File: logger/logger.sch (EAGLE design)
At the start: 18 parts, among them IC1 75176AD, U1 MSP430G2352IPW14

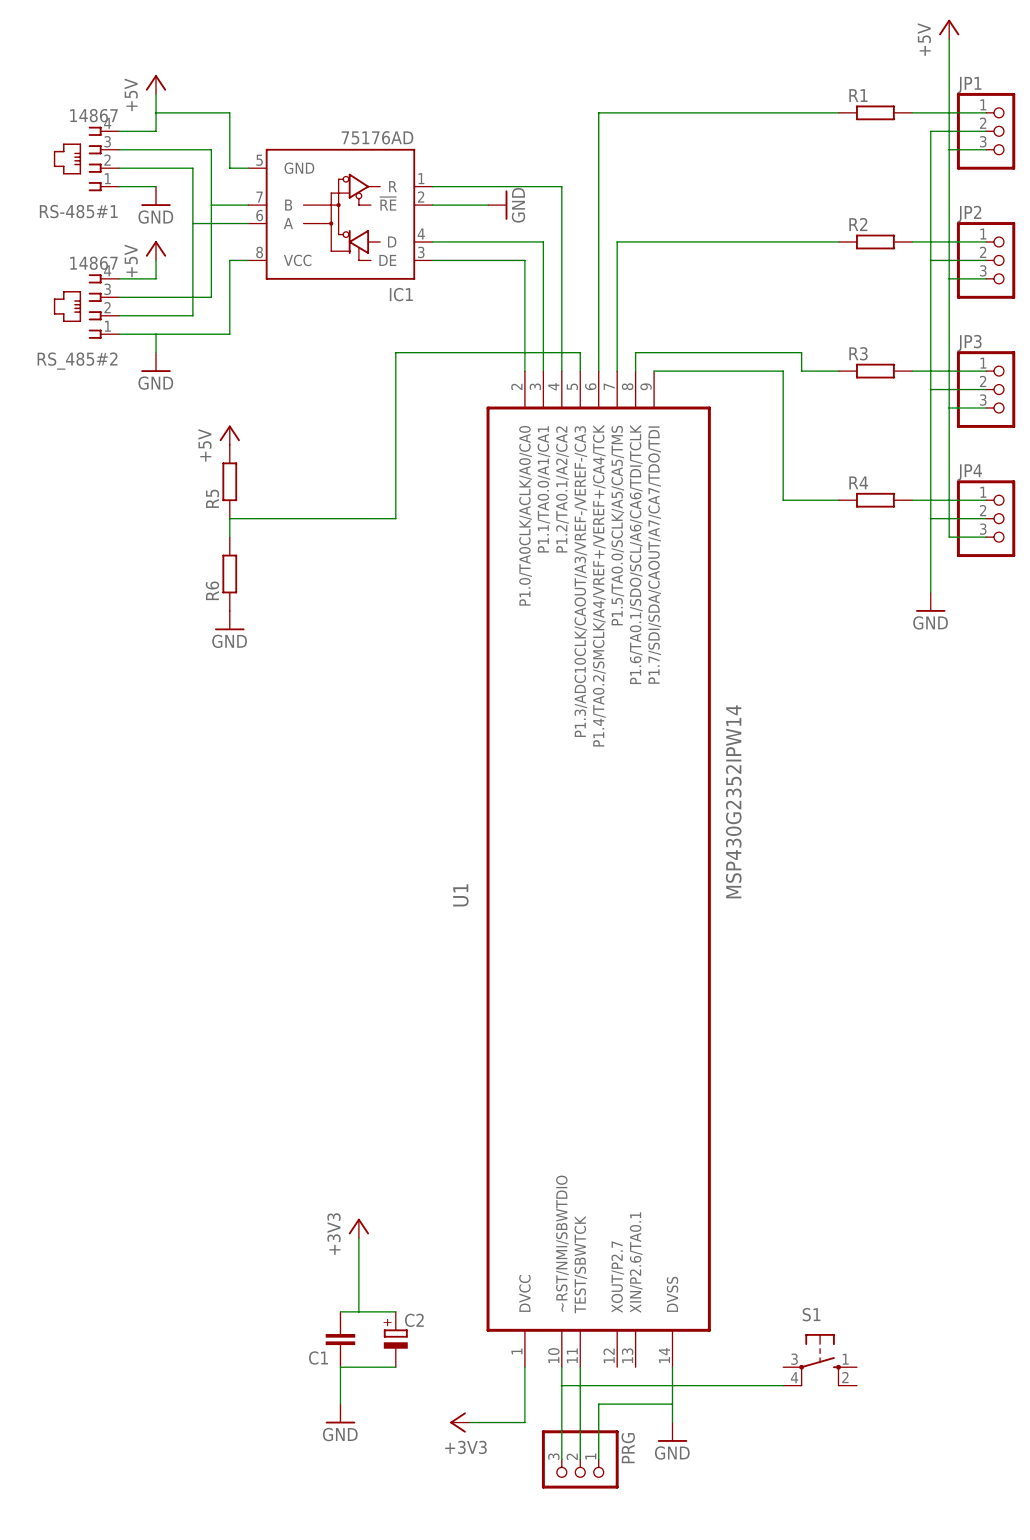
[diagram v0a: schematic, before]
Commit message: Bugfixes, partially routed.
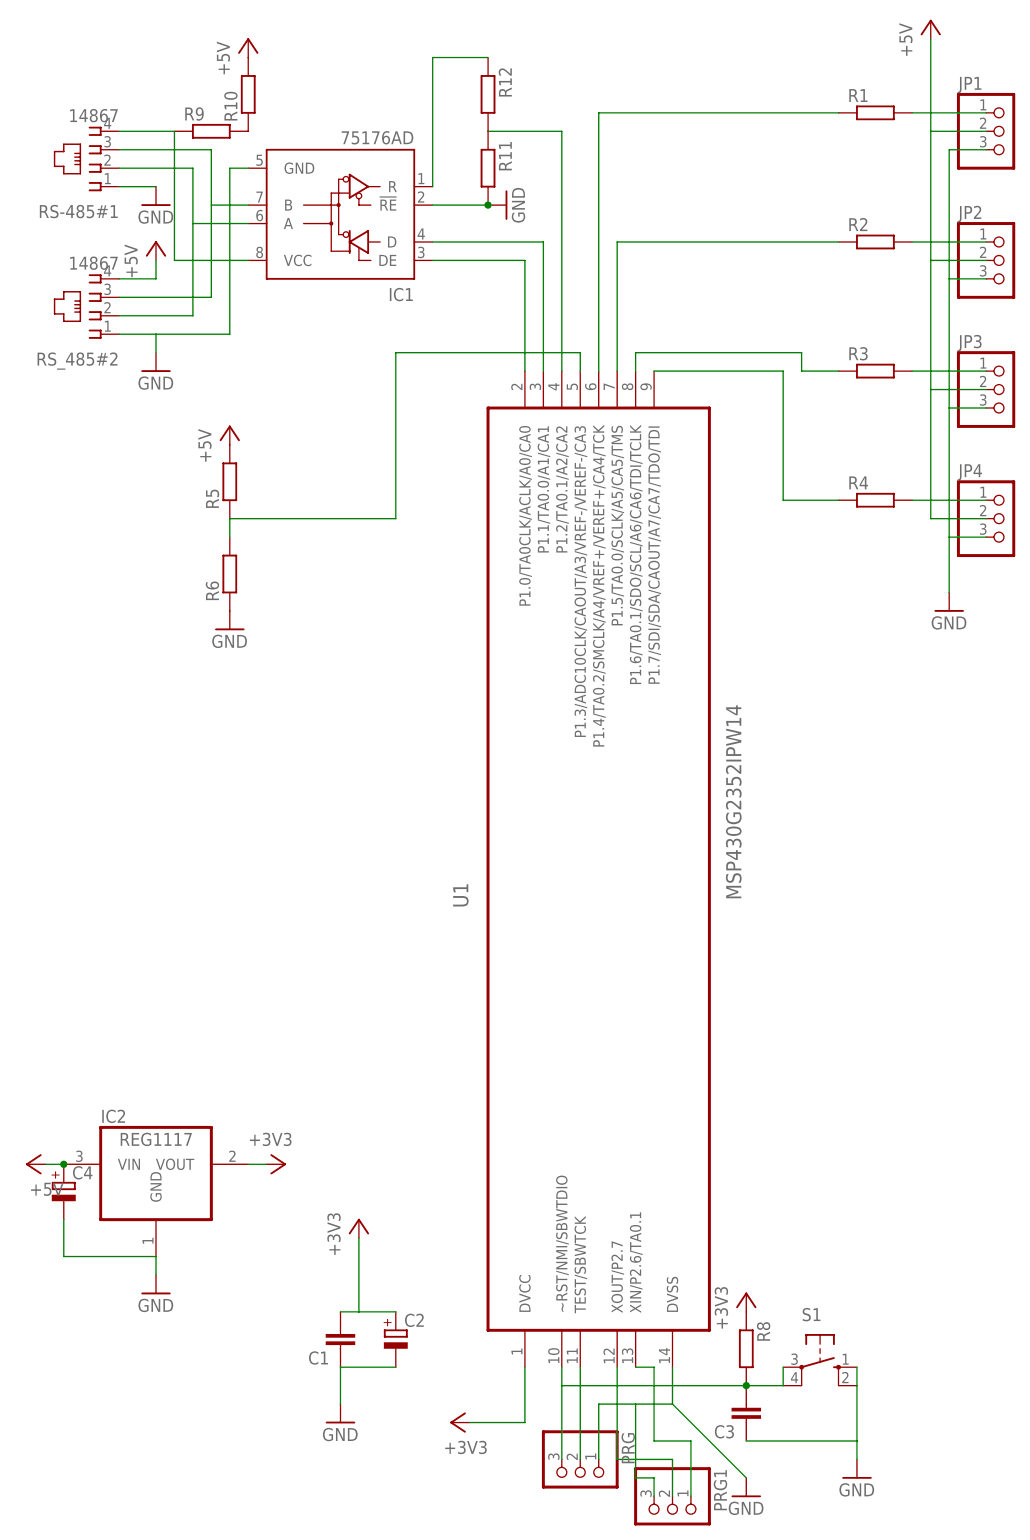
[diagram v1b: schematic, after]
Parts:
- added C3: (no value), rcl:C-EUC0805
- added C4: (no value), rcl:CPOL-EUE2,5-6E
- added IC2: REG1117, burr-brown:REG1117
- added PRG1: (no value), pinhead:PINHD-1X3
- added R10, R9: (no value), rcl:R-EU_R1206
- added R11, R12, R8: (no value), rcl:R-EU_R0805
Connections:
- removed net N$12: IC1.R, U1.P1.2/TA0.1/A2/CA2
- new net N$17: PRG1.1, U1.XIN/P2.6/TA0.1
- new net N$18: PRG1.2, U1.XOUT/P2.7
- new net N$19: R10.1, R9.2
- new net N$20: IC1.VCC, R9.1, RS-485#1.4
- new net N$21: IC1.R, R12.1
- new net N$22: R11.1, R12.2, U1.P1.2/TA0.1/A2/CA2
- net +3V3: now also IC2.VOUT, R8.1
- net +5V: now also C4.+, IC2.VIN, JP1.2, JP2.2, JP3.2, JP4.2, R10.2; no longer IC1.GND, JP1.3, JP2.3, JP3.3, JP4.3, RS-485#1.4
- net GND: now also C3.1, C4.-, IC1.GND, IC2.GND, JP1.3, JP2.3, JP3.3, JP4.3, PRG1.3, R11.2, S1.S, S1.S1; no longer IC1.VCC, JP1.2, JP2.2, JP3.2, JP4.2
- net N$15: now also C3.2, R8.2, S1.P

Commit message: Routed.
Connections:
- removed net N$17: PRG1.1, U1.XIN/P2.6/TA0.1
- new net N$12: PRG1.2, U1.XIN/P2.6/TA0.1
- net +3V3: now also IC2.VOUT_P
- net GND: now also PRG1.1; no longer PRG1.3
- net N$18: now also PRG1.3; no longer PRG1.2
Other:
- moved on the sheet: C1, C2
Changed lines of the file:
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@@
 <part name="C1" library="rcl" deviceset="C-EU" device="C0805"/>
 <part name="C2" library="rcl" deviceset="CPOL-EU" device="E2,5-6E"/>
-<part name="+3V2" library="supply1" deviceset="+3V3" device=""/>
-<part name="GND7" library="supply1" deviceset="GND" device=""/>
 <part name="PRG" library="pinhead" deviceset="PINHD-1X3" device=""/>
 <part name="S1" library="switch-omron" deviceset="10-XX" device=""/>
@@
 <part name="R11" library="rcl" deviceset="R-EU_" device="R0805"/>
 <part name="R12" library="rcl" deviceset="R-EU_" device="R0805"/>
+<part name="C4" library="rcl" deviceset="CPOL-EU" device="E2,5-6E"/>
 <part name="IC2" library="burr-brown" deviceset="REG1117" device=""/>
-<part name="C4" library="rcl" deviceset="CPOL-EU" device="E2,5-6E"/>
 </parts>
 <sheets>
@@
 <instance part="+3V1" gate="G$1" x="40.64" y="-104.14" rot="R90"/>
 <instance part="GND6" gate="1" x="48.26" y="63.5" rot="R90"/>
-<instance part="C1" gate="G$1" x="25.4" y="-93.98" rot="R180"/>
-<instance part="C2" gate="G$1" x="33.02" y="-91.44"/>
-<instance part="+3V2" gate="G$1" x="27.94" y="-76.2"/>
-<instance part="GND7" gate="1" x="25.4" y="-104.14"/>
+<instance part="C1" gate="G$1" x="22.86" y="-73.66" rot="R180"/>
+<instance part="C2" gate="G$1" x="27.94" y="-71.12"/>
 <instance part="PRG" gate="A" x="58.42" y="-111.76" rot="R270"/>
 <instance part="S1" gate="1" x="91.44" y="-96.52" rot="R270"/>
 <instance part="GND8" gate="1" x="0" y="-86.36"/>
-<instance part="+3V3" gate="G$1" x="17.78" y="-68.58" rot="R270"/>
+<instance part="+3V3" gate="G$1" x="30.48" y="-68.58" rot="R270"/>
 <instance part="P+5" gate="1" x="-17.78" y="-68.58" rot="R90"/>
 <instance part="R8" gate="G$1" x="81.28" y="-93.98" rot="R270"/>
@@
 <instance part="R11" gate="G$1" x="45.72" y="68.58" rot="R270"/>
 <instance part="R12" gate="G$1" x="45.72" y="78.74" rot="R270"/>
+<instance part="C4" gate="G$1" x="-12.7" y="-71.12"/>
 <instance part="IC2" gate="G$1" x="0" y="-68.58"/>
-<instance part="C4" gate="G$1" x="-12.7" y="-71.12"/>
 </instances>
 <busses>
@@
 <segment>
 <pinref part="P+5" gate="1" pin="+5V"/>
-<pinref part="IC2" gate="G$1" pin="VIN"/>
 <wire x1="-15.24" y1="-68.58" x2="-12.7" y2="-68.58" width="0.1524" layer="91"/>
 <pinref part="C4" gate="G$1" pin="+"/>
+<pinref part="IC2" gate="G$1" pin="VIN"/>
 <junction x="-12.7" y="-68.58"/>
 </segment>
@@
 <wire x1="71.12" y1="-96.52" x2="71.12" y2="-101.6" width="0.1524" layer="91"/>
 <pinref part="PRG" gate="A" pin="1"/>
-<wire x1="71.12" y1="-101.6" x2="81.28" y2="-111.76" width="0.1524" layer="91"/>
+<wire x1="71.12" y1="-101.6" x2="73.66" y2="-104.14" width="0.1524" layer="91"/>
+<wire x1="73.66" y1="-104.14" x2="81.28" y2="-111.76" width="0.1524" layer="91"/>
 <wire x1="60.96" y1="-109.22" x2="60.96" y2="-101.6" width="0.1524" layer="91"/>
-<wire x1="60.96" y1="-101.6" x2="66.04" y2="-101.6" width="0.1524" layer="91"/>
-<pinref part="PRG1" gate="A" pin="3"/>
-<wire x1="66.04" y1="-101.6" x2="71.12" y2="-101.6" width="0.1524" layer="91"/>
-<wire x1="68.58" y1="-114.3" x2="68.58" y2="-111.76" width="0.1524" layer="91"/>
-<wire x1="68.58" y1="-111.76" x2="66.04" y2="-111.76" width="0.1524" layer="91"/>
-<wire x1="66.04" y1="-111.76" x2="66.04" y2="-101.6" width="0.1524" layer="91"/>
+<wire x1="60.96" y1="-101.6" x2="71.12" y2="-101.6" width="0.1524" layer="91"/>
+<pinref part="PRG1" gate="A" pin="1"/>
+<wire x1="73.66" y1="-114.3" x2="73.66" y2="-104.14" width="0.1524" layer="91"/>
 </segment>
 <segment>
@@
 <pinref part="R11" gate="G$1" pin="2"/>
 <junction x="45.72" y="63.5"/>
-</segment>
-<segment>
-<pinref part="C1" gate="G$1" pin="1"/>
-<pinref part="C2" gate="G$1" pin="-"/>
-<wire x1="25.4" y1="-96.52" x2="33.02" y2="-96.52" width="0.1524" layer="91"/>
-<pinref part="GND7" gate="1" pin="GND"/>
-<wire x1="25.4" y1="-96.52" x2="25.4" y2="-101.6" width="0.1524" layer="91"/>
 </segment>
 <segment>
@@
 </segment>
 <segment>
-<pinref part="IC2" gate="G$1" pin="GND"/>
 <pinref part="GND8" gate="1" pin="GND"/>
 <wire x1="0" y1="-81.28" x2="0" y2="-83.82" width="0.1524" layer="91"/>
@@
 <wire x1="0" y1="-81.28" x2="-12.7" y2="-81.28" width="0.1524" layer="91"/>
 <wire x1="-12.7" y1="-81.28" x2="-12.7" y2="-76.2" width="0.1524" layer="91"/>
+<pinref part="C1" gate="G$1" pin="1"/>
+<wire x1="0" y1="-81.28" x2="22.86" y2="-81.28" width="0.1524" layer="91"/>
+<wire x1="22.86" y1="-81.28" x2="22.86" y2="-76.2" width="0.1524" layer="91"/>
+<pinref part="C2" gate="G$1" pin="-"/>
+<wire x1="22.86" y1="-81.28" x2="27.94" y2="-81.28" width="0.1524" layer="91"/>
+<wire x1="27.94" y1="-81.28" x2="27.94" y2="-76.2" width="0.1524" layer="91"/>
+<pinref part="IC2" gate="G$1" pin="GND"/>
+<junction x="0" y="-81.28"/>
 </segment>
 </net>
@@
 </segment>
 <segment>
-<pinref part="C1" gate="G$1" pin="2"/>
-<pinref part="+3V2" gate="G$1" pin="+3V3"/>
-<wire x1="25.4" y1="-88.9" x2="27.94" y2="-88.9" width="0.1524" layer="91"/>
-<wire x1="27.94" y1="-88.9" x2="27.94" y2="-78.74" width="0.1524" layer="91"/>
-<pinref part="C2" gate="G$1" pin="+"/>
-<wire x1="27.94" y1="-88.9" x2="33.02" y2="-88.9" width="0.1524" layer="91"/>
-</segment>
-<segment>
 <pinref part="R8" gate="G$1" pin="1"/>
 <pinref part="+3V4" gate="G$1" pin="+3V3"/>
 </segment>
 <segment>
+<pinref part="C2" gate="G$1" pin="+"/>
+<pinref part="+3V3" gate="G$1" pin="+3V3"/>
+<pinref part="C1" gate="G$1" pin="2"/>
+<wire x1="12.7" y1="-68.58" x2="17.78" y2="-68.58" width="0.1524" layer="91"/>
+<wire x1="27.94" y1="-68.58" x2="17.78" y2="-68.58" width="0.1524" layer="91"/>
 <pinref part="IC2" gate="G$1" pin="VOUT"/>
-<pinref part="+3V3" gate="G$1" pin="+3V3"/>
-<wire x1="12.7" y1="-68.58" x2="15.24" y2="-68.58" width="0.1524" layer="91"/>
+<wire x1="17.78" y1="-68.58" x2="22.86" y2="-68.58" width="0.1524" layer="91"/>
+<junction x="17.78" y="-68.58"/>
+<pinref part="IC2" gate="G$1" pin="VOUT_P"/>
+<wire x1="17.78" y1="-71.12" x2="17.78" y2="-68.58" width="0.1524" layer="91"/>
 </segment>
 </net>
@@
 </segment>
 </net>
-<net name="N$17" class="0">
-<segment>
-<pinref part="U1" gate="A" pin="XIN/P2.6/TA0.1"/>
-<wire x1="66.04" y1="-96.52" x2="68.58" y2="-96.52" width="0.1524" layer="91"/>
-<wire x1="68.58" y1="-96.52" x2="68.58" y2="-106.68" width="0.1524" layer="91"/>
-<pinref part="PRG1" gate="A" pin="1"/>
-<wire x1="68.58" y1="-106.68" x2="73.66" y2="-106.68" width="0.1524" layer="91"/>
-<wire x1="73.66" y1="-106.68" x2="73.66" y2="-114.3" width="0.1524" layer="91"/>
-</segment>
-</net>
 <net name="N$18" class="0">
 <segment>
-<pinref part="PRG1" gate="A" pin="2"/>
-<wire x1="71.12" y1="-114.3" x2="71.12" y2="-109.22" width="0.1524" layer="91"/>
 <pinref part="U1" gate="A" pin="XOUT/P2.7"/>
-<wire x1="71.12" y1="-109.22" x2="63.5" y2="-109.22" width="0.1524" layer="91"/>
 <wire x1="63.5" y1="-109.22" x2="63.5" y2="-96.52" width="0.1524" layer="91"/>
+<pinref part="PRG1" gate="A" pin="3"/>
+<wire x1="63.5" y1="-109.22" x2="68.58" y2="-109.22" width="0.1524" layer="91"/>
+<wire x1="68.58" y1="-109.22" x2="68.58" y2="-114.3" width="0.1524" layer="91"/>
 </segment>
 </net>
@@
 </segment>
 </net>
+<net name="N$12" class="0">
+<segment>
+<pinref part="U1" gate="A" pin="XIN/P2.6/TA0.1"/>
+<wire x1="66.04" y1="-96.52" x2="68.58" y2="-96.52" width="0.1524" layer="91"/>
+<pinref part="PRG1" gate="A" pin="2"/>
+<wire x1="71.12" y1="-114.3" x2="71.12" y2="-106.68" width="0.1524" layer="91"/>
+<wire x1="71.12" y1="-106.68" x2="68.58" y2="-106.68" width="0.1524" layer="91"/>
+<wire x1="68.58" y1="-106.68" x2="68.58" y2="-96.52" width="0.1524" layer="91"/>
+</segment>
+</net>

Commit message: Final changes.
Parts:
- added JP5: (no value), pinhead:PINHD-1X1
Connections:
- net +3V3: now also JP5.1
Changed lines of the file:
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@@
 <part name="C4" library="rcl" deviceset="CPOL-EU" device="E2,5-6E"/>
 <part name="IC2" library="burr-brown" deviceset="REG1117" device=""/>
+<part name="JP5" library="pinhead" deviceset="PINHD-1X1" device=""/>
 </parts>
 <sheets>
@@
 <instance part="C4" gate="G$1" x="-12.7" y="-71.12"/>
 <instance part="IC2" gate="G$1" x="0" y="-68.58"/>
+<instance part="JP5" gate="G$1" x="50.8" y="-111.76" rot="R270"/>
 </instances>
 <busses>
@@
 <wire x1="43.18" y1="-104.14" x2="50.8" y2="-104.14" width="0.1524" layer="91"/>
 <wire x1="50.8" y1="-104.14" x2="50.8" y2="-96.52" width="0.1524" layer="91"/>
-</segment>
-<segment>
+<pinref part="JP5" gate="G$1" pin="1"/>
+<wire x1="50.8" y1="-104.14" x2="50.8" y2="-109.22" width="0.1524" layer="91"/>
+</segment>
+<segment>
